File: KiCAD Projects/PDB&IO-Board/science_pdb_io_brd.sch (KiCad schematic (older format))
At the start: 38 parts, among them P1 ROBOT_PWR_IN, P10 BB_Power, P11 ENCODER_1, P13 LIMIT1_IN, P14 LIMIT2_IN, P15 LIMIT3_IN, P16 ENCODER_3, P17 MOTOR1_PWM, P18 MOTOR2_PWM, P19 MOTOR3_PWM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

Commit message: Preparing for PCB Work
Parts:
- removed P1: ROBOT_PWR_IN, symbol CONN_01X02
- added C?: C, symbol C
- added D? (x2): LED, symbol LED
- added P?: CONN_01X04, symbol CONN_01X04
- added R? (x2): R, symbol R
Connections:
- wire segments 169 -> 183
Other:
- moved on the sheet: P8, R10, R11, R9

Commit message: Fixed net name labels
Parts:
- removed P10: BB_Power, symbol CONN_01X02
- added D3: LED, symbol LED
- added R17: R, Capacitors_SMD:C_1206_HandSoldering, symbol R
- C1, C2, C3, R1, R10, R11, R12, R13, R14, R2, R3, R4, R5, R6, R7, R8, R9: footprint (none) -> Capacitors_SMD:C_1206_HandSoldering
- C4: renamed from C?; footprint (none) -> Capacitors_SMD:C_1206_HandSoldering
- P1: renamed from P?; value CONN_01X04 -> MAIN_PWR_IN
- P5: value CONN_01X06 -> THERMO_SENS
- P6: value CONN_01X07 -> DIST_SENS
- P7: value CONN_01X05 -> UV_SENS
- R15, R16: renamed from R?; footprint (none) -> Capacitors_SMD:C_1206_HandSoldering
- U1: footprint (none) -> Housings_SOIC:SOIC-14_3.9x8.7mm_Pitch1.27mm
- gave numbers to parts that had none: 2
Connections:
- net labels added: +3.3V
- wire segments 183 -> 200
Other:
- moved on the sheet: P16, P2, P21, R1, R15, R16, R2, R6, R7, R8

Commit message: Worked some more on Power Distribution Board
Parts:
- removed D1: LED, symbol LED
- removed P1: MAIN_PWR_IN, symbol CONN_01X04
- removed P2: 12V-5V_REG, symbol CONN_01X03
- removed P9: MOTOR_PWR_OUT, symbol CONN_01X08
- removed R15: R, Capacitors_SMD:C_1206_HandSoldering, symbol R
- added P?: PWR_IN, symbol CONN_01X02
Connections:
- net labels removed: +12V, GND
- wire segments 200 -> 173
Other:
- moved on the sheet: R16, R17

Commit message: Made pin connetions for encoder
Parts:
- D2, D3: symbol LED -> LED-RESCUE-science_pdb_io_brd
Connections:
- wire segments 173 -> 182
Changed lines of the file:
@@
 EESchema Schematic File Version 2
+LIBS:science_pdb_io_brd-rescue
 LIBS:power
 LIBS:device
@@
 $EndComp
 $Comp
-L LED D2
+L LED-RESCUE-science_pdb_io_brd D2
 U 1 1 58BC1092
 P 1200 1550
@@
 	1    0    0    -1
 $EndComp
-$Comp
-L GNDD #PWR033
-U 1 1 58BC7CCF
-P 2800 7000
-F 0 "#PWR033" H 2800 6750 50  0001 C CNN
-F 1 "GNDD" H 2800 6850 50  0000 C CNN
-F 2 "" H 2800 7000 50  0000 C CNN
-F 3 "" H 2800 7000 50  0000 C CNN
-	1    2800 7000
-	1    0    0    -1
-$EndComp
 Wire Wire Line
 	2800 6900 2800 7050
@@
 $EndComp
 $Comp
-L LED D3
+L LED-RESCUE-science_pdb_io_brd D3
 U 1 1 58BF0CDA
 P 1550 1550
@@
 Wire Wire Line
 	2350 1150 2350 1250
+Wire Wire Line
+	10450 2600 10850 2600
+Wire Wire Line
+	10450 2500 10850 2500
+Wire Wire Line
+	10450 2300 10850 2300
+Wire Wire Line
+	10450 2200 10850 2200
+Wire Wire Line
+	10450 2000 10850 2000
+Wire Wire Line
+	10450 1900 10850 1900
+Text Label 10850 1900 2    40   ~ 0
+ENC1_A
+Text Label 10850 2000 2    40   ~ 0
+ENC1_B
+Text Label 10850 2200 2    40   ~ 0
+ENC2_A
+Text Label 10850 2300 2    40   ~ 0
+ENC2_B
+Text Label 10850 2500 2    40   ~ 0
+ENC3_A
+Text Label 10850 2600 2    40   ~ 0
+ENC3_B
+Wire Wire Line
+	10450 1800 10850 1800
+Wire Wire Line
+	10450 2100 10850 2100
+Wire Wire Line
+	10450 2400 10850 2400
+Text Label 10850 1800 2    40   ~ 0
+ENC1_BUT
+Text Label 10850 2100 2    40   ~ 0
+ENC2_BUT
+Text Label 10850 2400 2    40   ~ 0
+ENC3_BUT
+$Comp
+L GNDD #PWR?
+U 1 1 58D38FCA
+P 2800 7050
+F 0 "#PWR?" H 2800 6800 50  0001 C CNN
+F 1 "GNDD" H 2800 6900 50  0000 C CNN
+F 2 "" H 2800 7050 50  0000 C CNN
+F 3 "" H 2800 7050 50  0000 C CNN
+	1    2800 7050
+	1    0    0    -1
+$EndComp
 $EndSCHEMATC

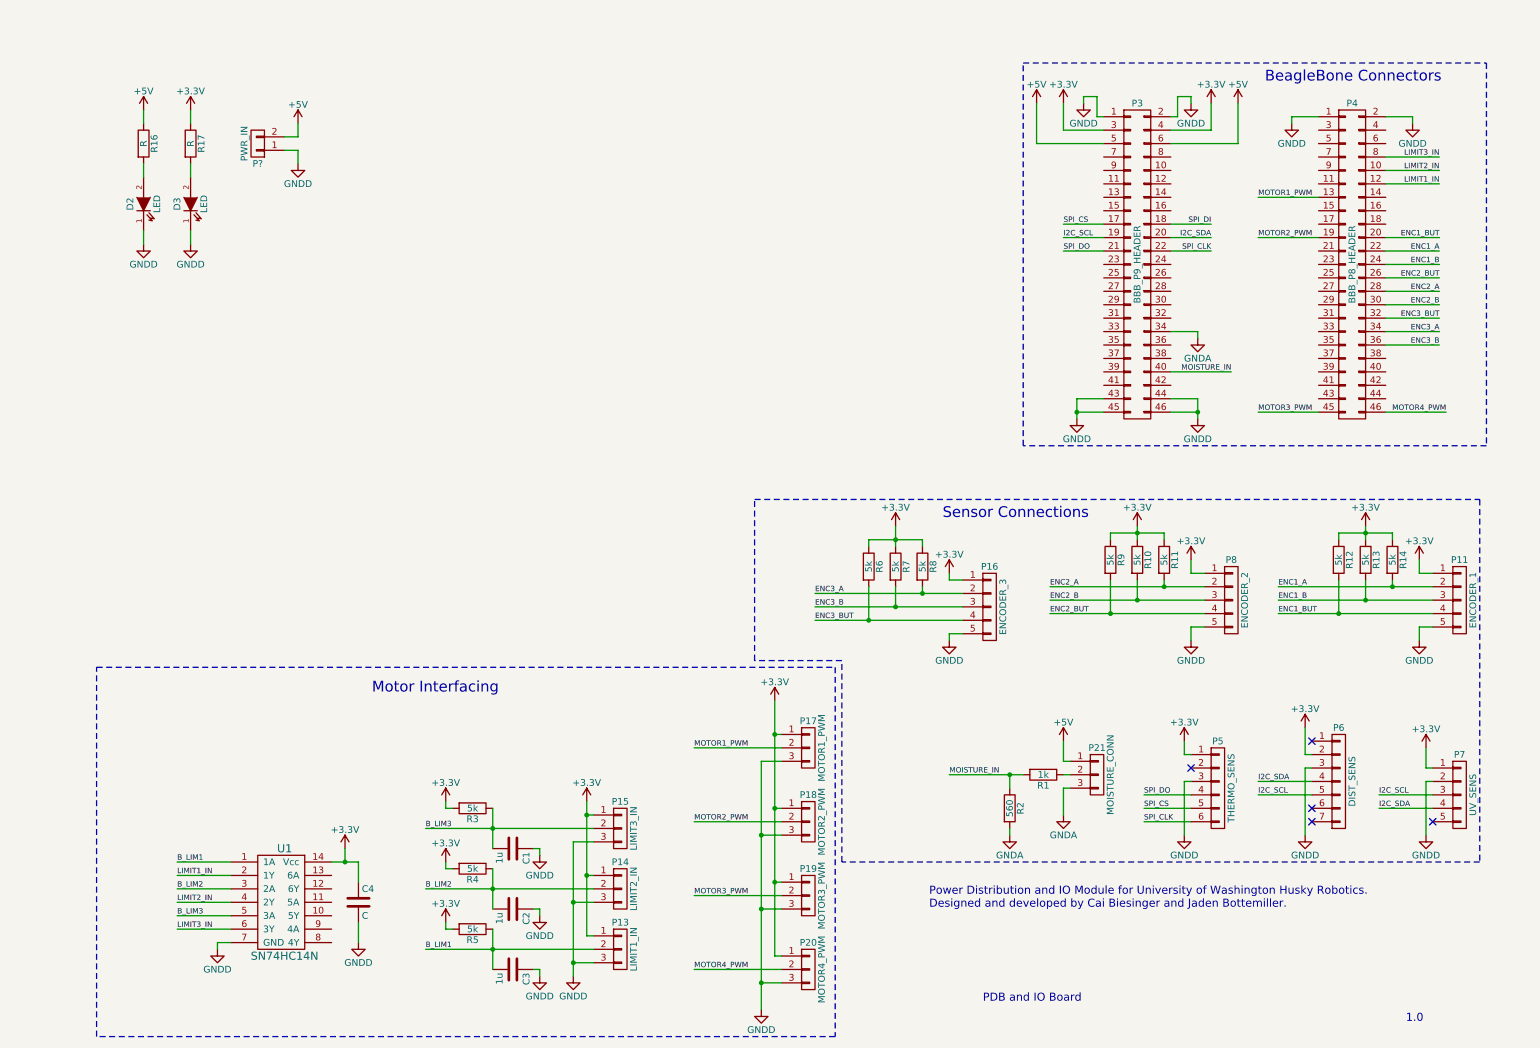
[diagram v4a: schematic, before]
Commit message: Added Pi Headers and Power and ground
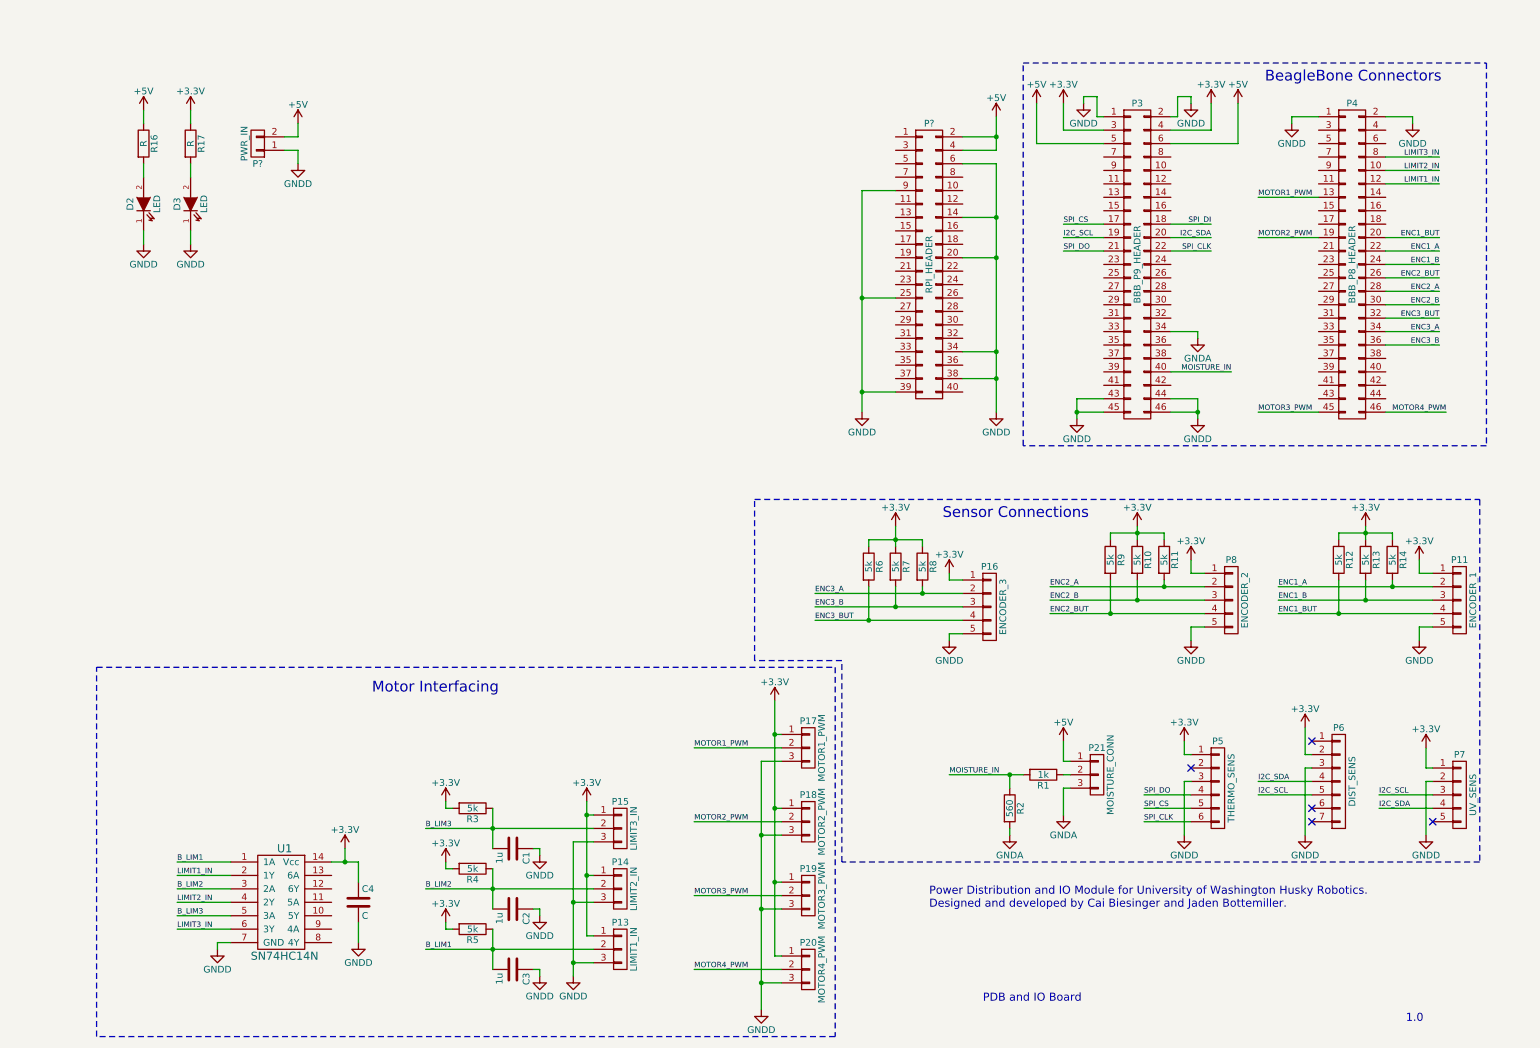
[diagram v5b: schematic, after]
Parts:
- added P?: RPI_HEADER, symbol CONN_02X20
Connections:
- net +5V: now also P?.2 (P2), P?.4 (P4)
- net GNDD: now also P?.14 (P14), P?.20 (P20), P?.25 (P25), P?.34 (P34), P?.38 (P38), P?.39 (P39), P?.6 (P6), P?.9 (P9)
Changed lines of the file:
@@
 Connection ~ 7650 5800
 Wire Wire Line
-	7200 5800 7750 5800
+	7200 5800 7650 5800
+Wire Wire Line
+	7650 5800 7750 5800
 Wire Wire Line
 	8050 5900 8050 6100
@@
 	5800 5700 5950 5700
 Wire Wire Line
-	5800 5700 5800 7550
+	5800 5700 5800 6250
+Wire Wire Line
+	5800 6250 5800 6800
+Wire Wire Line
+	5800 6800 5800 7350
+Wire Wire Line
+	5800 7350 5800 7550
 Wire Wire Line
 	5900 7150 5950 7150
 Wire Wire Line
-	5900 5250 5900 7150
-Wire Wire Line
-	3300 6200 4550 6200
-Wire Wire Line
-	3300 7100 4550 7100
+	5900 5250 5900 5500
+Wire Wire Line
+	5900 5500 5900 6050
+Wire Wire Line
+	5900 6050 5900 6600
+Wire Wire Line
+	5900 6600 5900 7150
+Wire Wire Line
+	3300 6200 3800 6200
+Wire Wire Line
+	3800 6200 4550 6200
+Wire Wire Line
+	3300 7100 3800 7100
+Wire Wire Line
+	3800 7100 4550 7100
 Connection ~ 4400 7200
 Wire Wire Line
@@
 	4500 7000 4550 7000
 Wire Wire Line
-	4500 6000 4500 7000
+	4500 6000 4500 6100
+Wire Wire Line
+	4500 6100 4500 6550
+Wire Wire Line
+	4500 6550 4500 7000
 Wire Wire Line
 	4400 6300 4550 6300
 Wire Wire Line
-	4400 6300 4400 7300
+	4400 6300 4400 6750
+Wire Wire Line
+	4400 6750 4400 7200
+Wire Wire Line
+	4400 7200 4400 7300
 Wire Wire Line
 	8950 5850 8950 6250
@@
 	1450 6950 1850 6950
 Wire Wire Line
-	2600 6450 2800 6450
+	2600 6450 2700 6450
+Wire Wire Line
+	2700 6450 2800 6450
 Wire Wire Line
 	2700 6450 2700 6350
@@
 Connection ~ 3800 6200
 Wire Wire Line
-	3800 6500 3800 6800
-Wire Wire Line
-	3800 6950 3800 7250
+	3800 6500 3800 6650
+Wire Wire Line
+	3800 6650 3800 6800
+Wire Wire Line
+	3800 6950 3800 7100
+Wire Wire Line
+	3800 7100 3800 7250
 Connection ~ 3800 7100
 Wire Notes Line
@@
 	4150 6800 4100 6800
 Wire Wire Line
-	3300 6650 4550 6650
+	3300 6650 3800 6650
+Wire Wire Line
+	3800 6650 4550 6650
 Connection ~ 3800 6650
 Wire Wire Line
-	3800 6050 3800 6350
+	3800 6050 3800 6200
+Wire Wire Line
+	3800 6200 3800 6350
 Wire Wire Line
 	4150 6400 4150 6350
@@
 	8650 5950 9000 5950
 Wire Wire Line
-	8150 3000 8150 3150
+	8150 3000 8150 3100
+Wire Wire Line
+	8150 3100 8150 3150
 Wire Wire Line
 	8150 3100 8350 3100
@@
 	8850 3100 9050 3100
 Wire Wire Line
-	9050 3000 9050 3150
+	9050 3000 9050 3100
+Wire Wire Line
+	9050 3100 9050 3150
 Wire Wire Line
 	8350 3000 8150 3000
@@
 	7200 4750 7200 4800
 Wire Wire Line
-	6200 4450 7300 4450
-Wire Wire Line
-	6200 4550 7300 4550
-Wire Wire Line
-	6200 4650 7300 4650
+	6200 4450 7000 4450
+Wire Wire Line
+	7000 4450 7300 4450
+Wire Wire Line
+	6200 4550 6800 4550
+Wire Wire Line
+	6800 4550 7300 4550
+Wire Wire Line
+	6200 4650 6600 4650
+Wire Wire Line
+	6600 4650 7300 4650
 Wire Wire Line
 	6600 4400 6600 4650
@@
 	10700 4700 10700 4800
 Wire Wire Line
-	9650 4400 10800 4400
-Wire Wire Line
-	9650 4500 10800 4500
-Wire Wire Line
-	9650 4600 10800 4600
+	9650 4400 10500 4400
+Wire Wire Line
+	10500 4400 10800 4400
+Wire Wire Line
+	9650 4500 10300 4500
+Wire Wire Line
+	10300 4500 10800 4500
+Wire Wire Line
+	9650 4600 10100 4600
+Wire Wire Line
+	10100 4600 10800 4600
 Wire Wire Line
 	10100 4350 10100 4600
@@
 Connection ~ 10300 4500
 Wire Wire Line
-	10300 3950 10300 4050
+	10300 3950 10300 4000
+Wire Wire Line
+	10300 4000 10300 4050
 Wire Wire Line
 	9000 4300 9100 4300
@@
 	9000 4700 9000 4800
 Wire Wire Line
-	7950 4400 9100 4400
-Wire Wire Line
-	7950 4600 9100 4600
+	7950 4400 8800 4400
+Wire Wire Line
+	8800 4400 9100 4400
+Wire Wire Line
+	7950 4600 8400 4600
+Wire Wire Line
+	8400 4600 9100 4600
 Wire Wire Line
 	8400 4350 8400 4600
@@
 	6600 4050 6600 4100
 Wire Wire Line
-	6600 4050 7000 4050
-Wire Wire Line
-	6800 3950 6800 4100
+	6600 4050 6800 4050
+Wire Wire Line
+	6800 4050 7000 4050
+Wire Wire Line
+	6800 3950 6800 4050
+Wire Wire Line
+	6800 4050 6800 4100
 Wire Wire Line
 	7000 4050 7000 4100
 Connection ~ 6800 4050
 Wire Wire Line
-	10100 4000 10500 4000
+	10100 4000 10300 4000
+Wire Wire Line
+	10300 4000 10500 4000
 Wire Wire Line
 	10500 4000 10500 4050
@@
 $EndComp
 Wire Wire Line
-	8400 4000 8800 4000
+	8400 4000 8600 4000
+Wire Wire Line
+	8600 4000 8800 4000
 Wire Wire Line
 	8800 4000 8800 4050
 Wire Wire Line
-	8600 3950 8600 4050
+	8600 3950 8600 4000
+Wire Wire Line
+	8600 4000 8600 4050
 Connection ~ 8600 4000
 Wire Wire Line
@@
 Connection ~ 7000 4450
 Wire Wire Line
-	7950 4500 9100 4500
+	7950 4500 8600 4500
+Wire Wire Line
+	8600 4500 9100 4500
 Wire Wire Line
 	8800 4350 8800 4400
@@
 	1    0    0    -1
 $EndComp
+$Comp
+L CONN_02X20 P?
+U 1 1 58E16CB5
+P 7050 2000
+F 0 "P?" H 7050 3050 50  0000 C CNN
+F 1 "RPI_HEADER" V 7050 2000 50  0000 C CNN
+F 2 "" H 7050 1050 50  0000 C CNN
+F 3 "" H 7050 1050 50  0000 C CNN
+	1    7050 2000
+	1    0    0    -1
+$EndComp
+Wire Wire Line
+	7300 1050 7550 1050
+Wire Wire Line
+	7550 900  7550 1050
+Wire Wire Line
+	7550 1050 7550 1150
+Wire Wire Line
+	7300 1250 7550 1250
+Wire Wire Line
+	6800 1450 6550 1450
+Wire Wire Line
+	6550 1450 6550 2250
+Wire Wire Line
+	6550 2250 6550 2950
+Wire Wire Line
+	6550 2950 6550 3100
+Wire Wire Line
+	6550 2250 6800 2250
+Wire Wire Line
+	6550 2950 6800 2950
+Wire Wire Line
+	7300 2650 7550 2650
+Wire Wire Line
+	7550 1250 7550 1650
+Wire Wire Line
+	7550 1650 7550 1950
+Wire Wire Line
+	7550 1950 7550 2650
+Wire Wire Line
+	7550 2650 7550 2850
+Wire Wire Line
+	7550 2850 7550 3100
+Wire Wire Line
+	7300 2850 7550 2850
+Connection ~ 7550 2850
+Wire Wire Line
+	7300 1950 7550 1950
+Connection ~ 7550 2650
+Connection ~ 7550 1950
+Wire Wire Line
+	7300 1650 7550 1650
+Connection ~ 7550 1650
+Wire Wire Line
+	7550 1150 7300 1150
+Connection ~ 7550 1050
+Connection ~ 6550 2250
+Connection ~ 6550 2950
+$Comp
+L +5V #PWR?
+U 1 1 58E197A2
+P 7550 900
+F 0 "#PWR?" H 7550 750 50  0001 C CNN
+F 1 "+5V" H 7550 1040 50  0000 C CNN
+F 2 "" H 7550 900 50  0000 C CNN
+F 3 "" H 7550 900 50  0000 C CNN
+	1    7550 900
+	1    0    0    -1
+$EndComp
+$Comp
+L GNDD #PWR?
+U 1 1 58E19808
+P 7550 3100
+F 0 "#PWR?" H 7550 2850 50  0001 C CNN
+F 1 "GNDD" H 7550 2950 50  0000 C CNN
+F 2 "" H 7550 3100 50  0000 C CNN
+F 3 "" H 7550 3100 50  0000 C CNN
+	1    7550 3100
+	1    0    0    -1
+$EndComp
+$Comp
+L GNDD #PWR?
+U 1 1 58E19895
+P 6550 3100
+F 0 "#PWR?" H 6550 2850 50  0001 C CNN
+F 1 "GNDD" H 6550 2950 50  0000 C CNN
+F 2 "" H 6550 3100 50  0000 C CNN
+F 3 "" H 6550 3100 50  0000 C CNN
+	1    6550 3100
+	1    0    0    -1
+$EndComp

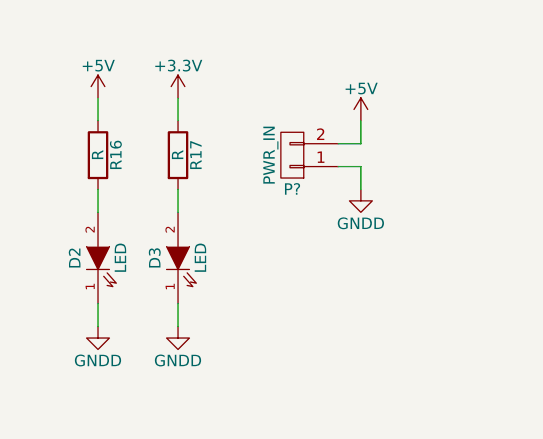
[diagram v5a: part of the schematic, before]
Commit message: Added current limiting resistors to 5V and 3.3V
On IO board only
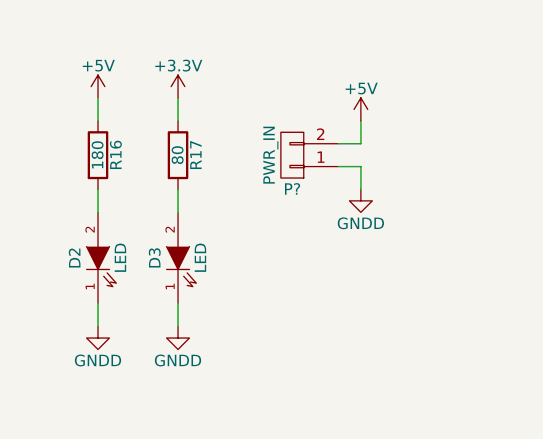
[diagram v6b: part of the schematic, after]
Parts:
- R16: value R -> 180
- R17: value R -> 80
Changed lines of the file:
@@
 P 1200 1100
 F 0 "R16" V 1280 1100 50  0000 C CNN
-F 1 "R" V 1200 1100 50  0000 C CNN
+F 1 "180" V 1200 1100 50  0000 C CNN
 F 2 "Capacitors_SMD:C_1206_HandSoldering" V 1130 1100 50  0001 C CNN
 F 3 "" H 1200 1100 50  0000 C CNN
@@
 P 1550 1100
 F 0 "R17" V 1630 1100 50  0000 C CNN
-F 1 "R" V 1550 1100 50  0000 C CNN
+F 1 "80" V 1550 1100 50  0000 C CNN
 F 2 "Capacitors_SMD:C_1206_HandSoldering" V 1480 1100 50  0001 C CNN
 F 3 "" H 1550 1100 50  0000 C CNN

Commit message: Worked on Main Board
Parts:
- C1, C2, C3: value 1u -> 1μF
- P2: renamed from P?; footprint (none) -> Pin_Headers:Pin_Header_Straight_2x20_Pitch2.54mm
- R1: value 1k -> 1kΩ
- R10, R11, R12, R13, R14, R3, R4, R5, R6, R7, R8, R9: value 5k -> 5kΩ
- R16: value 180 -> 180Ω
- R17: value 80 -> 80Ω
- R2: value 560 -> 560Ω
- gave numbers to parts that had none: 1
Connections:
- net CAM_TRIG: now reaches P3.15 (P15)
- net CAM_TRIG: now also P2.16 (P16)
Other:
- moved on the sheet: P2

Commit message: Last main PCB commit for now.
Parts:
- D2, D3: footprint (none) -> LEDs:LED_D5.0mm
- P11, P16, P8: footprint (none) -> Pin_Headers:Pin_Header_Straight_1x05_Pitch2.54mm
- P13, P14, P15, P17, P18, P19, P20, P21: footprint (none) -> Pin_Headers:Pin_Header_Straight_1x03_Pitch2.54mm
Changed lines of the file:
@@
 F 0 "P15" H 4750 6400 50  0000 C CNN
 F 1 "LIMIT3_IN" V 4850 6200 50  0000 C CNN
-F 2 "" H 4750 6200 50  0001 C CNN
+F 2 "Pin_Headers:Pin_Header_Straight_1x03_Pitch2.54mm" H 4750 6200 50  0001 C CNN
 F 3 "" H 4750 6200 50  0000 C CNN
 	1    4750 6200
@@
 F 0 "P14" H 4750 6850 50  0000 C CNN
 F 1 "LIMIT2_IN" V 4850 6650 50  0000 C CNN
-F 2 "" H 4750 6650 50  0001 C CNN
+F 2 "Pin_Headers:Pin_Header_Straight_1x03_Pitch2.54mm" H 4750 6650 50  0001 C CNN
 F 3 "" H 4750 6650 50  0000 C CNN
 	1    4750 6650
@@
 F 0 "P13" H 4750 7300 50  0000 C CNN
 F 1 "LIMIT1_IN" V 4850 7100 50  0000 C CNN
-F 2 "" H 4750 7100 50  0001 C CNN
+F 2 "Pin_Headers:Pin_Header_Straight_1x03_Pitch2.54mm" H 4750 7100 50  0001 C CNN
 F 3 "" H 4750 7100 50  0000 C CNN
 	1    4750 7100
@@
 F 0 "P16" H 7500 4850 50  0000 C CNN
 F 1 "ENCODER_3" V 7600 4550 50  0000 C CNN
-F 2 "" H 7500 4550 50  0001 C CNN
+F 2 "Pin_Headers:Pin_Header_Straight_1x05_Pitch2.54mm" H 7500 4550 50  0001 C CNN
 F 3 "" H 7500 4550 50  0000 C CNN
 	1    7500 4550
@@
 F 0 "P20" H 6150 7450 50  0000 C CNN
 F 1 "MOTOR4_PWM" V 6250 7250 50  0000 C CNN
-F 2 "" H 6150 7250 50  0001 C CNN
+F 2 "Pin_Headers:Pin_Header_Straight_1x03_Pitch2.54mm" H 6150 7250 50  0001 C CNN
 F 3 "" H 6150 7250 50  0000 C CNN
 	1    6150 7250
@@
 F 0 "P19" H 6150 6900 50  0000 C CNN
 F 1 "MOTOR3_PWM" V 6250 6700 50  0000 C CNN
-F 2 "" H 6150 6700 50  0001 C CNN
+F 2 "Pin_Headers:Pin_Header_Straight_1x03_Pitch2.54mm" H 6150 6700 50  0001 C CNN
 F 3 "" H 6150 6700 50  0000 C CNN
 	1    6150 6700
@@
 F 0 "P18" H 6150 6350 50  0000 C CNN
 F 1 "MOTOR2_PWM" V 6250 6150 50  0000 C CNN
-F 2 "" H 6150 6150 50  0001 C CNN
+F 2 "Pin_Headers:Pin_Header_Straight_1x03_Pitch2.54mm" H 6150 6150 50  0001 C CNN
 F 3 "" H 6150 6150 50  0000 C CNN
 	1    6150 6150
@@
 F 0 "P17" H 6150 5800 50  0000 C CNN
 F 1 "MOTOR1_PWM" V 6250 5600 50  0000 C CNN
-F 2 "" H 6150 5600 50  0001 C CNN
+F 2 "Pin_Headers:Pin_Header_Straight_1x03_Pitch2.54mm" H 6150 5600 50  0001 C CNN
 F 3 "" H 6150 5600 50  0000 C CNN
 	1    6150 5600
@@
 F 0 "P21" H 8300 6000 50  0000 C CNN
 F 1 "MOISTURE_CONN" V 8400 5800 50  0000 C CNN
-F 2 "" H 8300 5800 50  0001 C CNN
+F 2 "Pin_Headers:Pin_Header_Straight_1x03_Pitch2.54mm" H 8300 5800 50  0001 C CNN
 F 3 "" H 8300 5800 50  0000 C CNN
 	1    8300 5800
@@
 F 0 "P11" H 11000 4800 50  0000 C CNN
 F 1 "ENCODER_1" V 11100 4500 50  0000 C CNN
-F 2 "" H 11000 4500 50  0001 C CNN
+F 2 "Pin_Headers:Pin_Header_Straight_1x05_Pitch2.54mm" H 11000 4500 50  0001 C CNN
 F 3 "" H 11000 4500 50  0000 C CNN
 	1    11000 4500
@@
 F 0 "P8" H 9300 4800 50  0000 C CNN
 F 1 "ENCODER_2" V 9400 4500 50  0000 C CNN
-F 2 "" H 9300 4500 50  0001 C CNN
+F 2 "Pin_Headers:Pin_Header_Straight_1x05_Pitch2.54mm" H 9300 4500 50  0001 C CNN
 F 3 "" H 9300 4500 50  0000 C CNN
 	1    9300 4500
@@
 F 0 "D2" H 1200 1650 50  0000 C CNN
 F 1 "LED" H 1200 1450 50  0000 C CNN
-F 2 "" H 1200 1550 50  0001 C CNN
+F 2 "LEDs:LED_D5.0mm" H 1200 1550 50  0001 C CNN
 F 3 "" H 1200 1550 50  0000 C CNN
 	1    1200 1550
@@
 F 0 "D3" H 1550 1650 50  0000 C CNN
 F 1 "LED" H 1550 1450 50  0000 C CNN
-F 2 "" H 1550 1550 50  0001 C CNN
+F 2 "LEDs:LED_D5.0mm" H 1550 1550 50  0001 C CNN
 F 3 "" H 1550 1550 50  0000 C CNN
 	1    1550 1550
